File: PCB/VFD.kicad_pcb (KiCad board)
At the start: 2 copper layers, 247 x 90.9 mm, 85 parts, among them J1 XLR3_Ground, J10 Conn_01x01, J11 Conn_01x01, J2 XLR3_Ground, J3 Conn_01x03_Male, J4 Conn_02x09_Odd_Even, J5 Conn_02x09_Odd_Even, J6 Conn_01x03_Male, J7 Conn_01x01, J8 Conn_01x01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

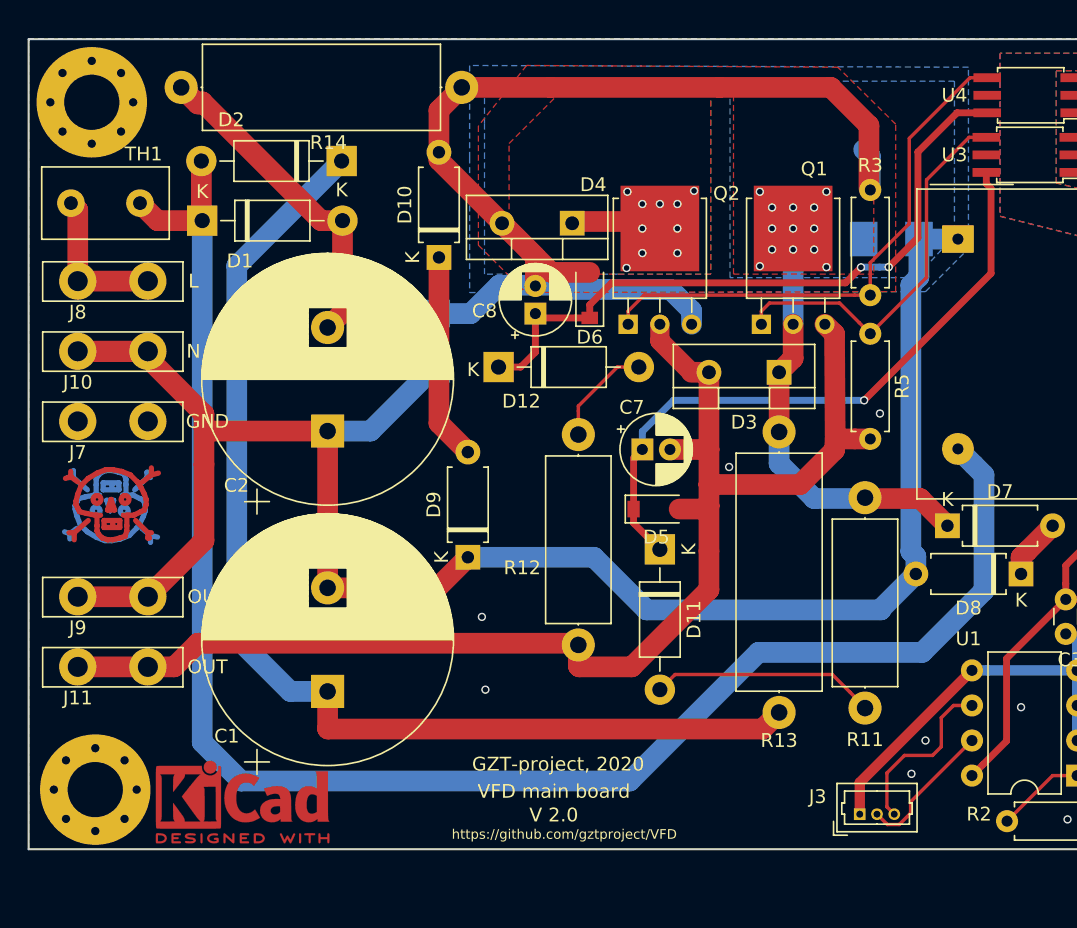
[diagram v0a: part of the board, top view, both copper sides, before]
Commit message: Added some more inductive surge protection
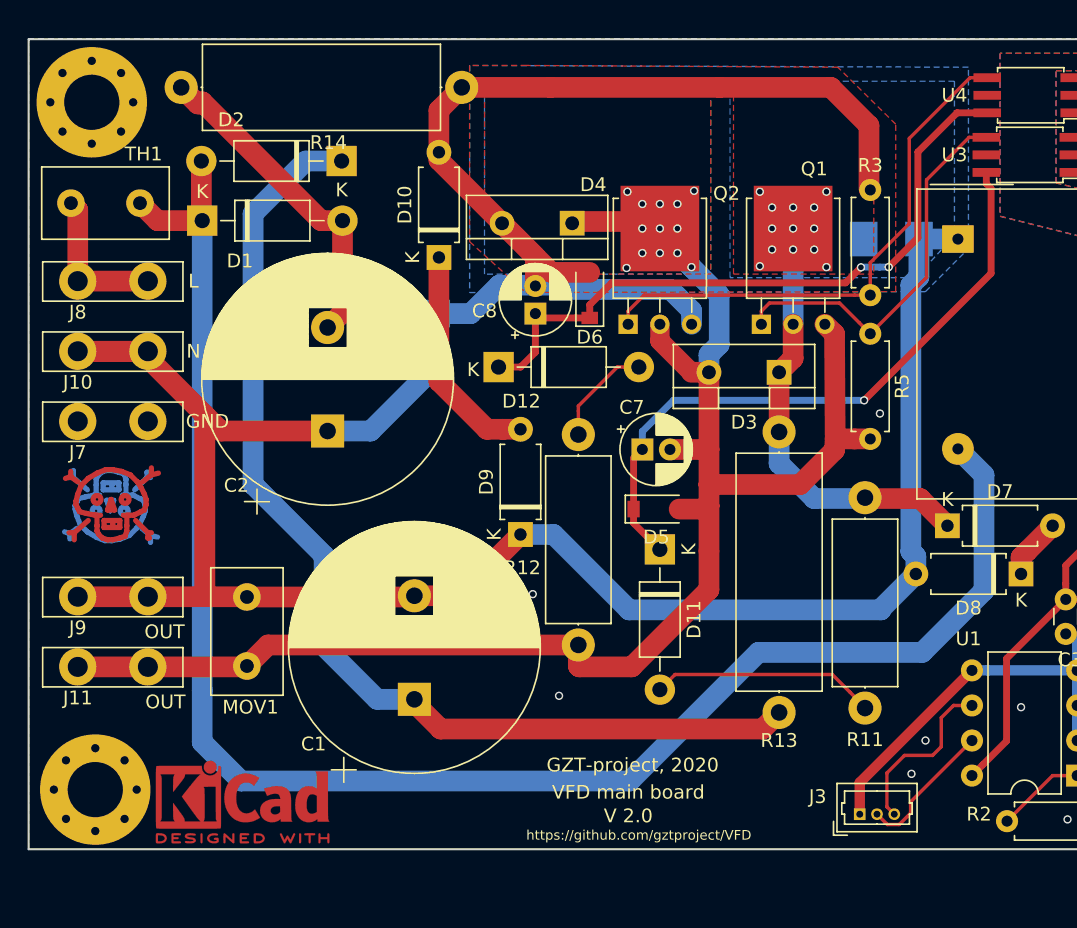
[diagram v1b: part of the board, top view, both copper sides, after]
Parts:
- added MOV1: 650V, Capacitor_THT:C_Disc_D9.0mm_W5.0mm_P5.00mm, F.Cu at (52.1, 80.2)
- moved C1 6.31 mm to (64.3, 82.6)
- moved D9 4.15 mm to (71.9, 70.7)
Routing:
- net /MotL: track 105.3 -> 115.3 mm, vias 10 -> 13
- net /+400V: track 81.8 -> 77.5 mm
- net /-IGBT: track 84.9 -> 81.8 mm
- net NEUT: track 139.9 -> 141.8 mm
- net Net-(D10-Pad1): track 15.0 -> 16.3 mm
- net GNDPWR: vias 12 -> 11

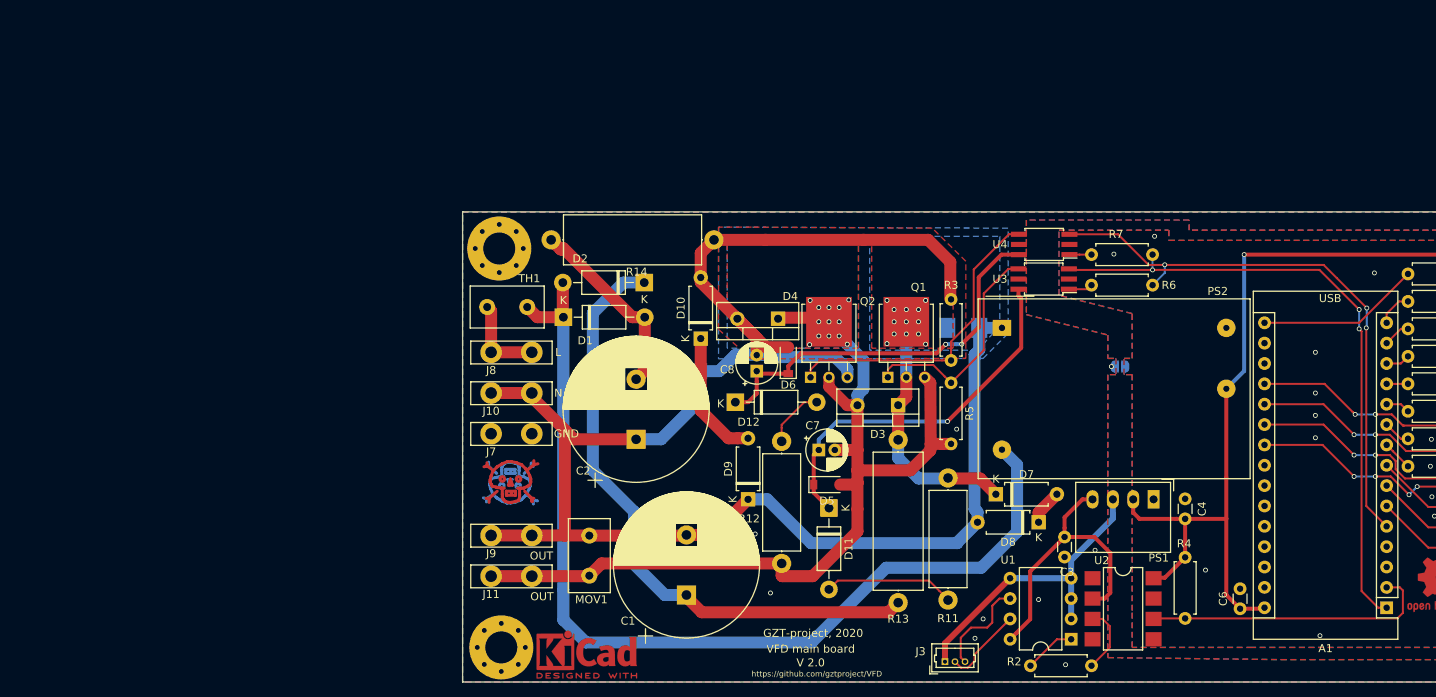
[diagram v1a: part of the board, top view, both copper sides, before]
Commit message: Started reworking the PCB layout
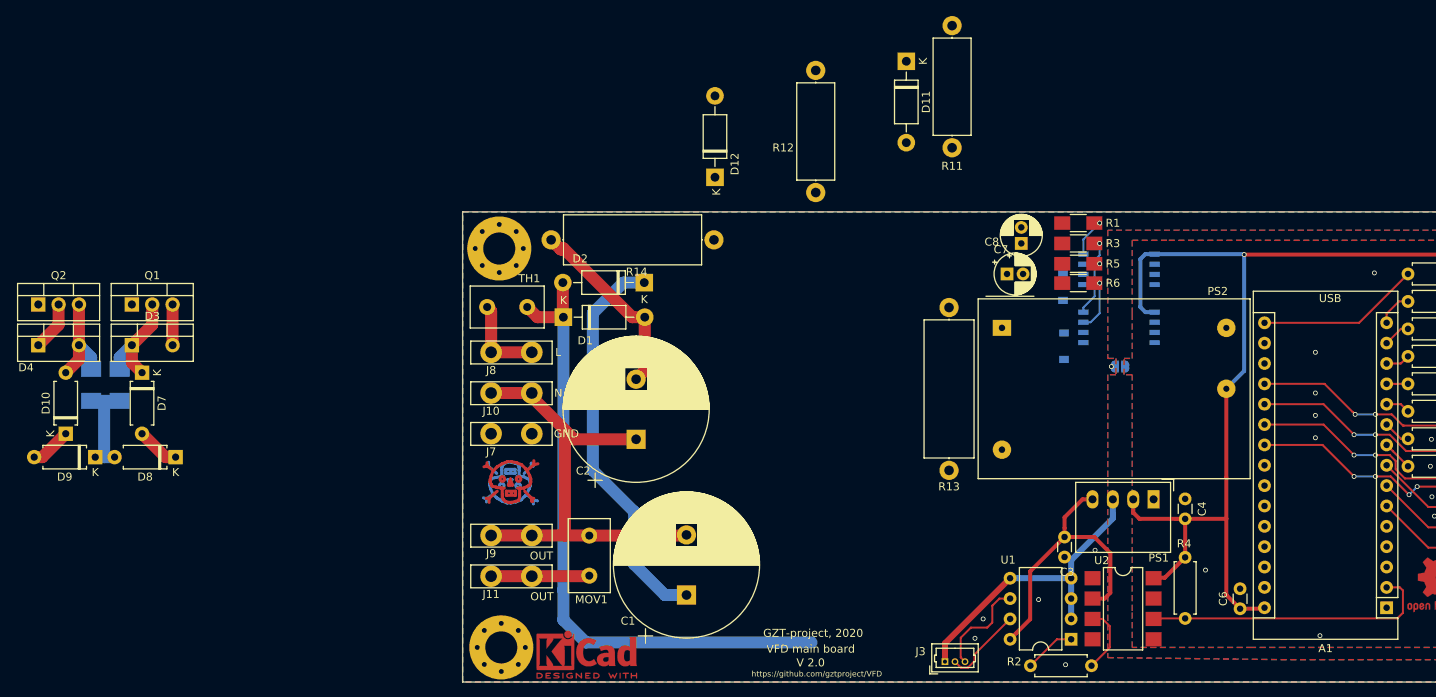
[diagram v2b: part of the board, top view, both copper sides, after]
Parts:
- removed R7: 120, Resistor_THT:R_Axial_DIN0207_L6.3mm_D2.5mm_P7.62mm_Horizontal
- added R1: 3R3, Resistors_SMD:R_1206_HandSoldering, F.Cu at (113.2, 36.2)
- D5, D6: moved to B.Cu
- Q1, Q2: value STGD5NB120SZ -> IXA12IF1200PB; footprint TO_SOT_Packages_THT:TO-251-3-1EP_IPAK_Horizontal -> TO_SOT_Packages_THT:TO-220-3_Vertical
- R3: value 22k -> 10R; footprint Resistor_THT:R_Axial_DIN0207_L6.3mm_D2.5mm_P7.62mm_Horizontal -> Resistors_SMD:R_1206_HandSoldering
- R5: value 22k -> 3R3; footprint Resistor_THT:R_Axial_DIN0207_L6.3mm_D2.5mm_P7.62mm_Horizontal -> Resistors_SMD:R_1206_HandSoldering
- R6: value 120 -> 10R; footprint Resistor_THT:R_Axial_DIN0207_L6.3mm_D2.5mm_P7.62mm_Horizontal -> Resistors_SMD:R_1206_HandSoldering
- U3, U4: value TLP185 -> 1EDIxxI12AH; footprint Housings_SOIC:SO-6_4.4x3.6mm_Pitch1.27mm -> Housings_SOIC:Infineon_PG-DSO-8-59; moved to B.Cu
- moved D8 108.0 mm to (0.51, 65.4)
- moved D7 107.6 mm to (-3.68, 54.9), turned to 270 degrees
- moved C5 105.5 mm to (-6.48, 56.4), turned to 270 degrees
- moved Q2 96.8 mm to (-16.6, 46.4)
- moved D3 95.9 mm to (-4.95, 51.4), turned to 0 degrees
- moved Q1 94.8 mm to (-4.95, 46.4)
- moved D4 92.4 mm to (-16.6, 51.4), turned to 0 degrees
- moved D9 81.6 mm to (-9.53, 65.4), turned to 180 degrees
- moved D10 80.1 mm to (-13.2, 62.5)
- moved C9 75.6 mm to (-10.0, 56.4)
- moved D11 56.6 mm to (91.7, 16.0)
- moved R11 56.5 mm to (97.4, 26.8)
- moved R12 46.5 mm to (80.4, 17.1)
- moved D5 38.4 mm to (111.3, 44.2), turned to 270 degrees
- moved C8 36.7 mm to (106.0, 38.7)
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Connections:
- D11 pad 1: /+OptoSupply -> /+IGBT
- D12 pad 1: /-OptoSupply -> /MotL
- R11 pad 2: /+IGBT -> /+OptoSupply
- R12 pad 2: /MotL -> /-OptoSupply
- R3 pad 1: /-Gate -> Net-(R3-Pad1)
- R3 pad 2: /-IGBT -> /+Gate
- R5 pad 1: /+Gate -> Net-(R5-Pad1)
- R5 pad 2: /MotL -> /-Gate
- R6 pad 1: /-Trig -> Net-(R6-Pad1)
- R6 pad 2: Net-(R6-Pad2) -> /-Gate
- U3 pad 1: Net-(R6-Pad2) -> +5V
- U3 pad 2: (no net) -> /+Trig
- U3 pad 3: /+Trig -> /-Trig
- U3 pad 4: /+Gate -> GND
- U3 pad 5: (no net) -> /MotL
- U4 pad 1: Net-(R7-Pad2) -> +5V
- U4 pad 2: (no net) -> /-Trig
- U4 pad 3: /-Trig -> /+Trig
- U4 pad 4: /-Gate -> GND
- U4 pad 5: (no net) -> /-IGBT
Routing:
- net /MotL: track 115.3 -> 23.5 mm, vias 13 -> 0
- net /+Trig: track 79.5 -> 0.00 mm, vias 3 -> 0
- net /-Trig: track 72.4 -> 0.00 mm, vias 3 -> 0
- net /-IGBT: track 81.8 -> 12.8 mm
- net NEUT: track 141.8 -> 76.3 mm
- net /-OptoSupply: track 49.1 -> 0.00 mm, vias 2 -> 0
- net /+OptoSupply: track 47.1 -> 0.00 mm, vias 1 -> 0
- net /L_NTC: track 121.7 -> 79.3 mm
- net /-Gate: track 39.0 -> 0.00 mm
- net /+Gate: track 28.4 -> 0.00 mm
- net /+400V: track 77.5 -> 49.8 mm
- net +5V: track 218.6 -> 239.9 mm
- net /+IGBT: track 31.5 -> 13.7 mm, vias 13 -> 0
- net Net-(D11-Pad2): track 16.5 -> 0.00 mm
- net Net-(D10-Pad1): track 16.3 -> 5.15 mm
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- removed copper zone on B.Cu, net /+IGBT
- removed copper zone on F.Cu, net /+IGBT
- removed copper zone on B.Cu, net /MotL
- removed copper zone on F.Cu, net /MotL

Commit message: More work on PCB
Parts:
- added C11: 1u, 25V, Capacitors_SMD:C_1206_HandSoldering, B.Cu at (111.5, 43.2)
- added C12: 1u, 25V, Capacitors_SMD:C_1206_HandSoldering, B.Cu at (111.5, 50.7)
- added C13: 100n, 25V, Capacitors_SMD:C_1206_HandSoldering, B.Cu at (125.0, 49.3)
- added C14: 100n, 25V, Capacitors_SMD:C_1206_HandSoldering, B.Cu at (125.0, 42.0)
- C3: footprint Capacitors_THT:C_Disc_D3.0mm_W1.6mm_P2.50mm -> Capacitors_SMD:C_1206_HandSoldering; moved to B.Cu
- C4: footprint Capacitors_THT:C_Disc_D3.0mm_W1.6mm_P2.50mm -> Capacitor_THT:CP_Radial_D5.0mm_P2.00mm
- C6: footprint Capacitors_THT:C_Disc_D3.0mm_W1.6mm_P2.50mm -> Capacitors_SMD:C_1206_HandSoldering
- D5, D6: value 10V -> 15V
- H8: footprint Mounting_Holes:MountingHole_4.3mm_M4_Pad_Via -> MountingHole:MountingHole_4mm_Pad_Via
- R10, R15, R16, R17, R18, R19, R2, R20, R21, R22, R4, R8, R9: footprint Resistor_THT:R_Axial_DIN0207_L6.3mm_D2.5mm_P7.62mm_Horizontal -> Resistors_THT:R_Axial_DIN0207_L6.3mm_D2.5mm_P7.62mm_Horizontal
- R11, R12: footprint Resistor_THT:R_Axial_DIN0414_L11.9mm_D4.5mm_P15.24mm_Horizontal -> Resistors_THT:R_Axial_DIN0414_L11.9mm_D4.5mm_P15.24mm_Horizontal
- R13, R14: footprint Resistor_THT:R_Axial_DIN0617_L17.0mm_D6.0mm_P20.32mm_Horizontal -> Resistors_THT:R_Axial_DIN0617_L17.0mm_D6.0mm_P20.32mm_Horizontal
- U1: footprint Package_DIP:DIP-8_W7.62mm -> Housings_DIP:DIP-8_W7.62mm
- moved C5 89.2 mm to (82.3, 48.1)
- moved C9 89.2 mm to (78.7, 48.1)
- moved D10 89.2 mm to (75.6, 54.2)
- moved D3 89.2 mm to (83.8, 43.2)
- moved D4 89.2 mm to (72.1, 43.2)
- moved D7 89.2 mm to (85.1, 46.6)
- moved Q1 89.2 mm to (83.8, 38.1)
- moved Q2 89.2 mm to (72.1, 38.1)
- moved D9 88.7 mm to (79.1, 61.8), turned to 90 degrees
- moved D8 85.0 mm to (85.1, 56.6), turned to 270 degrees
- moved D11 49.7 mm to (97.8, 65.3)
- moved R12 46.6 mm to (92.3, 62.2), turned to 90 degrees
- moved D12 42.6 mm to (92.3, 65.3), turned to 270 degrees
- moved R11 35.4 mm to (97.8, 62.2)
- moved R13 27.4 mm to (77.1, 65.5)
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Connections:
- net /+OptoSupply renamed /+DriverSupply
- net /+Trig renamed /Trig+
- net /-OptoSupply renamed /-DriverSupply
- net /-Trig renamed /Trig-
- D11 pad 1: /+IGBT -> Net-(D11-Pad1)
- D11 pad 2: Net-(D11-Pad2) -> /+IGBT
- D12 pad 1: /MotL -> Net-(D12-Pad1)
- D12 pad 2: Net-(D12-Pad2) -> /MotL
- R11 pad 1: Net-(D11-Pad2) -> Net-(D11-Pad1)
- R12 pad 1: Net-(D12-Pad2) -> Net-(D12-Pad1)
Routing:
- net /MotL: track 23.5 -> 162.3 mm
- net /Trig+: track 0.00 -> 66.9 mm, vias 0 -> 1
- net NEUT: track 76.3 -> 142.0 mm
- net /Trig-: track 0.00 -> 65.5 mm, vias 0 -> 1
- net /-IGBT: track 12.8 -> 68.9 mm
- net /+IGBT: track 13.7 -> 65.5 mm, vias 0 -> 2
- net /-Gate: track 0.00 -> 46.5 mm, vias 0 -> 2
- net /L_NTC: track 79.3 -> 121.3 mm
- net /+Gate: track 0.00 -> 30.6 mm
- net /-DriverSupply: track 0.00 -> 27.5 mm
- net /+DriverSupply: track 0.00 -> 19.0 mm
- net /+400V: track 49.8 -> 64.0 mm
- net Net-(D12-Pad1): track 0.00 -> 3.05 mm
- net Net-(D11-Pad1): track 0.00 -> 3.05 mm
- net +5VA: track 37.2 -> 40.2 mm
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- added copper zone on B.Cu, net /-IGBT
- added copper zone on B.Cu, net /MotL
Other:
- net class DriverSupply added: clearance 0.25, trace_width 0.5, via_dia 0.6, via_drill 0.4
- board text added: "V 3.0"
- board text removed: "V 2.0"

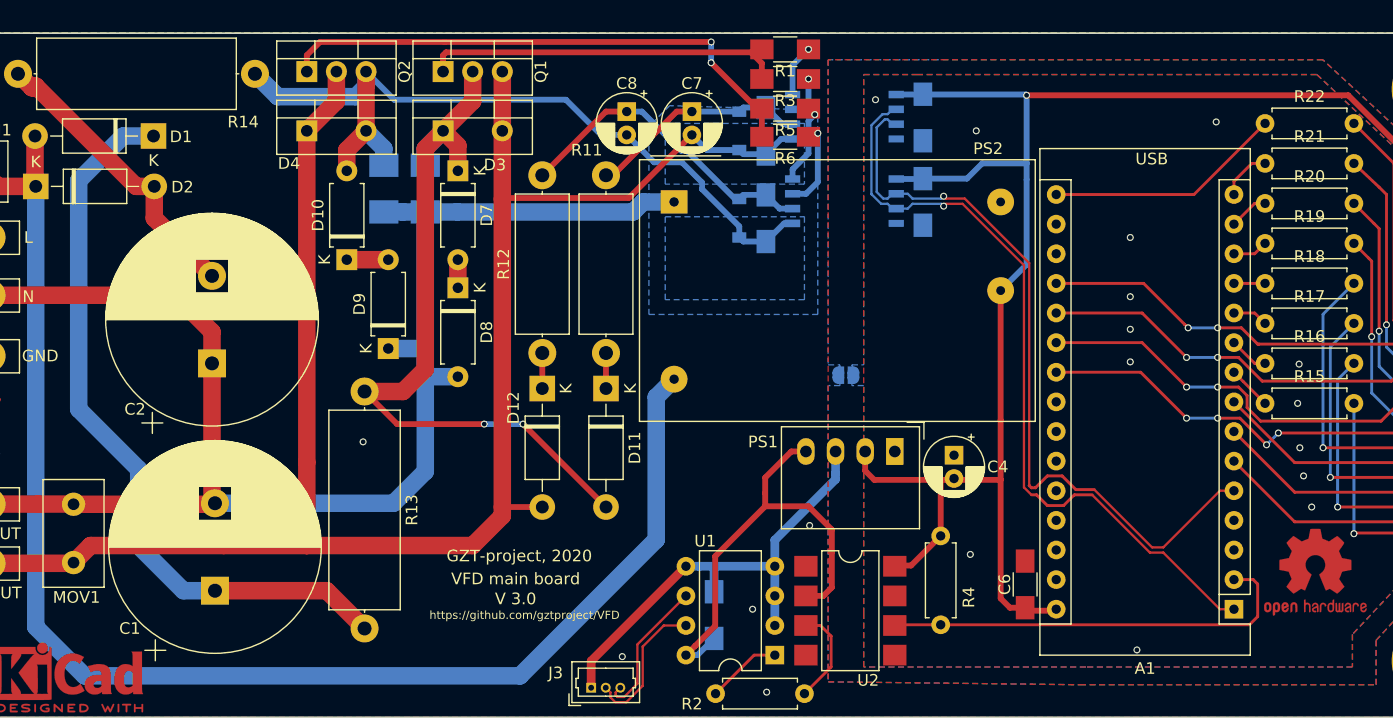
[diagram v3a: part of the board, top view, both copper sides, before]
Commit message: Added some testPoints
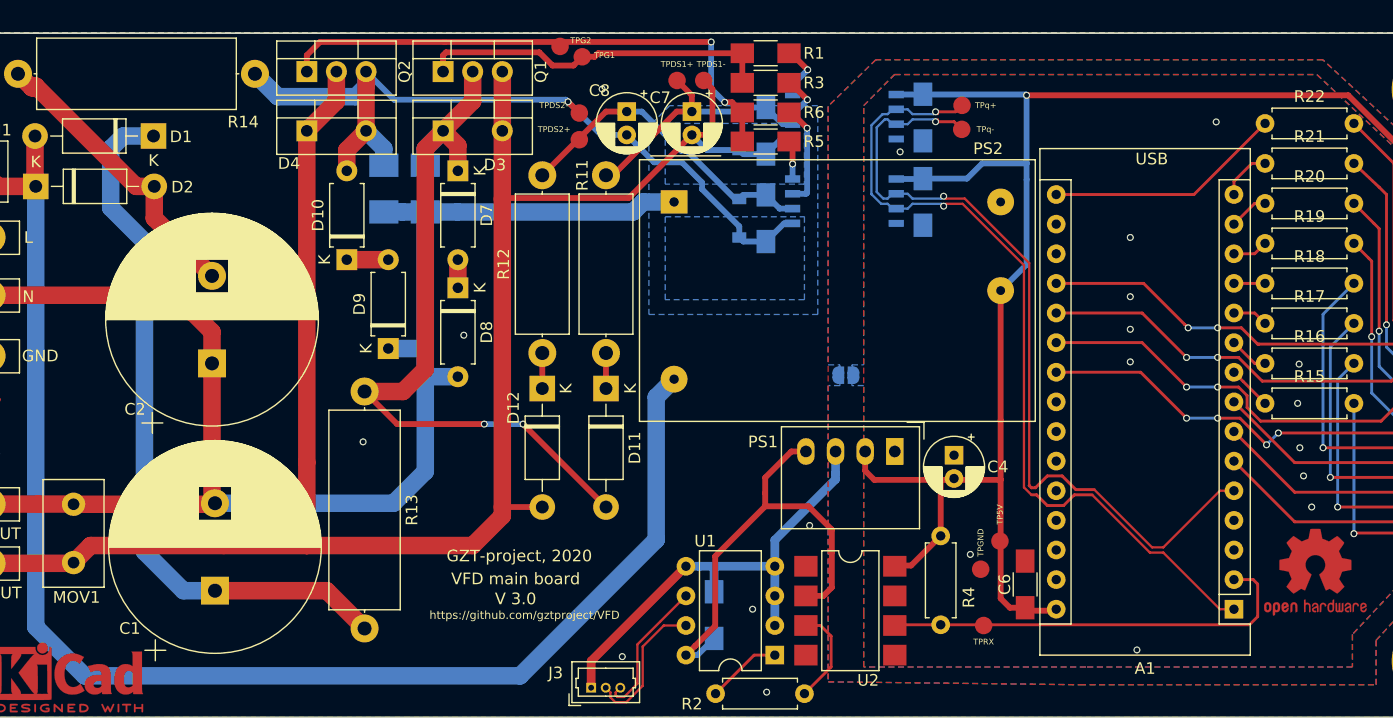
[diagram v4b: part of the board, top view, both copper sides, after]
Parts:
- added TP5V: Conn_01x01, Measurement_Points:Measurement_Point_Round-SMD-Pad_Small, F.Cu at (131.6, 78.4)
- added TPDS1+: Conn_01x01, Measurement_Points:Measurement_Point_Round-SMD-Pad_Small, F.Cu at (103.9, 38.9)
- added TPDS1-: Conn_01x01, Measurement_Points:Measurement_Point_Round-SMD-Pad_Small, F.Cu at (106.2, 38.9)
- added TPDS2+: Conn_01x01, Measurement_Points:Measurement_Point_Round-SMD-Pad_Small, F.Cu at (95.5, 43.9)
- added TPDS2-: Conn_01x01, Measurement_Points:Measurement_Point_Round-SMD-Pad_Small, F.Cu at (95.5, 41.7)
- added TPG1: Conn_01x01, Measurement_Points:Measurement_Point_Round-SMD-Pad_Small, F.Cu at (95.8, 36.8)
- added TPG2: Conn_01x01, Measurement_Points:Measurement_Point_Round-SMD-Pad_Small, F.Cu at (93.9, 35.9)
- added TPGND: Conn_01x01, Measurement_Points:Measurement_Point_Round-SMD-Pad_Small, F.Cu at (129.9, 80.8)
- added TPRX: Conn_01x01, Measurement_Points:Measurement_Point_Round-SMD-Pad_Small, F.Cu at (130.2, 85.6)
- added TPq+: Conn_01x01, Measurement_Points:Measurement_Point_Round-SMD-Pad_Small, F.Cu at (128.3, 41.0)
- added TPq-: Conn_01x01, Measurement_Points:Measurement_Point_Round-SMD-Pad_Small, F.Cu at (128.3, 43.1)
- moved R5 3.28 mm to (111.5, 44.1)
- moved R6 2.67 mm to (111.5, 41.6)
- moved R1 1.71 mm to (111.5, 36.5)
- moved R3 1.71 mm to (111.5, 39.1)
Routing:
- net /Trig-: track 65.5 -> 71.9 mm, vias 1 -> 2
- net /Trig+: track 66.9 -> 73.3 mm, vias 1 -> 2
- net /MotL: track 162.3 -> 168.7 mm
- net /+DriverSupply: track 19.0 -> 22.2 mm
- net Net-(R5-Pad1): track 6.31 -> 3.34 mm
- net /+400V: track 64.0 -> 61.7 mm
- net Net-(R6-Pad1): track 6.76 -> 8.93 mm
- net /-IGBT: track 68.9 -> 70.3 mm, vias 0 -> 1
- net GNDPWR: vias 7 -> 9
- net GND: vias 14 -> 13
